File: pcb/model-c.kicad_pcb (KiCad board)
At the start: 2 copper layers, 82 x 144.9 mm, 157 parts, among them IC1 HTK16K33, IC2 HTK16K33, J1 Batt, J2 Conn_01x02_Socket, J3 Conn_01x02_Socket, SW1 SW_SPST, SW10 SW_SPST, SW11 SW_SPST, SW12 SW_SPST, SW13 SW_SPST, SW14 SW_SPST, SW15 SW_SPST, SW16 SW_SPST, SW17 SW_SPST, SW18 SW_SPST, SW19 SW_SPST, SW2 SW_SPST, SW21 SW_SPDT, SW3 SW_SPST, SW4 SW_SPST, SW5 SW_SPST, SW6 SW_SPST, SW7 SW_SPST, SW8 SW_SPST, SW9 SW_SPST, U1 W25Q16JVUXIQ, U11 TPS63070RNMR, U2 14seg, U3 RP2040, U4 MCP73831-2-OT, U5 TPS61090, U6 14seg, U7 TLV75533PDBVR, U8 TPS2115APW, U9 TPS2115APW, Y1 12MHz

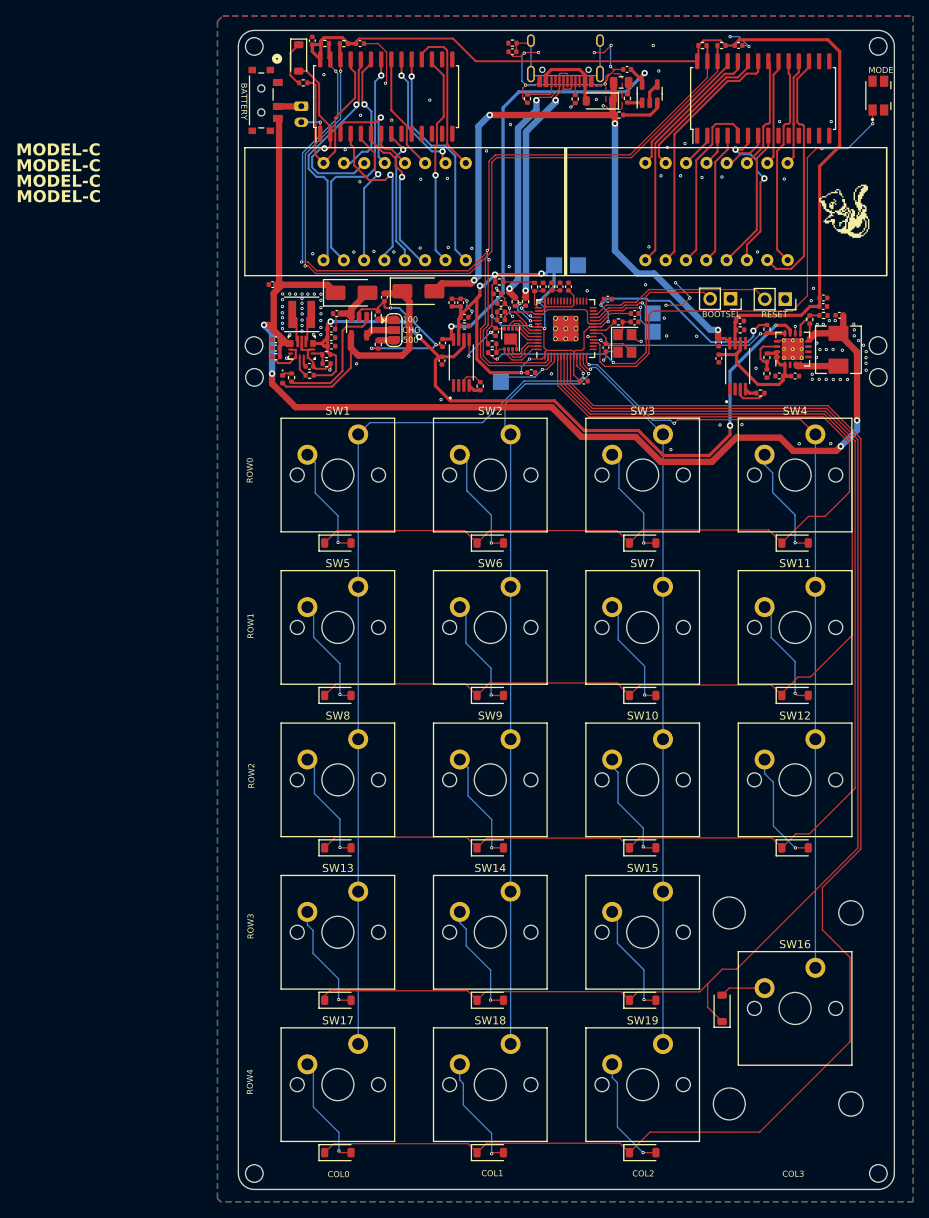
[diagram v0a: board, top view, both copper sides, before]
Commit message: housing complete and PCB validated. need further validation and revisions of housing, as well as BOM to continue. updated PCB to rev. 2.1
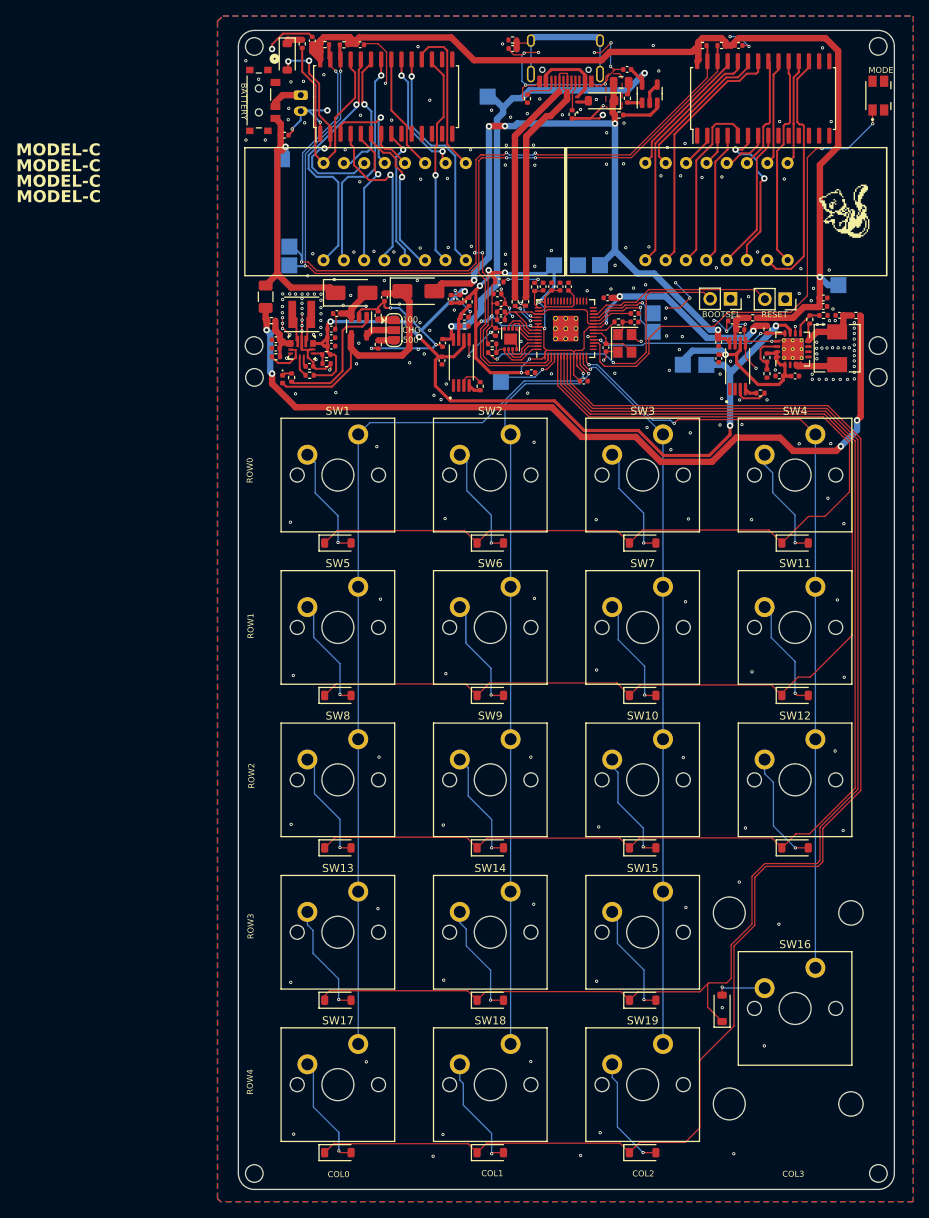
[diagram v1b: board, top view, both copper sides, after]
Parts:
- added D25: TPD1E05U06, footprints:RTVS_DFN1006-2_SOD882_NEX, F.Cu at (88.2, 33.3)
- added F2: Polyfuse_Small, Fuse:Fuse_1206_3216Metric, F.Cu at (49.2, 57.9)
- added FB2: FB, Resistor_SMD:R_0402_1005Metric, F.Cu at (110.1, 60.6)
- added FB3: FB, Resistor_SMD:R_0402_1005Metric, F.Cu at (74.7, 58.6)
- added FB4: FB, Resistor_SMD:R_0402_1005Metric, F.Cu at (123.0, 60.3)
- added FB5: FB, Resistor_SMD:R_0402_1005Metric, F.Cu at (50.0, 60.9)
- added TP10: TestPoint, libraries:CustomTestPoint, B.Cu at (104.3, 66.5)
- added TP11: TestPoint, libraries:CustomTestPoint, B.Cu at (120.8, 56.5)
- added TP12: TestPoint, libraries:CustomTestPoint, B.Cu at (52.2, 54.0)
- added TP13: TestPoint, libraries:CustomTestPoint, B.Cu at (52.2, 51.7)
- added TP5: TestPoint, libraries:CustomTestPoint, B.Cu at (51.3, 40.8)
- added TP6: TestPoint, libraries:CustomTestPoint, B.Cu at (91.0, 54.0)
- added TP7: TestPoint, libraries:CustomTestPoint, B.Cu at (77.0, 32.9)
- added TP8: TestPoint, libraries:CustomTestPoint, B.Cu at (101.4, 66.4)
- moved C20 18.7 mm to (51.6, 37.7), turned to 0 degrees
- moved R4 4.88 mm to (53.8, 26.3), turned to 90 degrees
- moved R6 1.96 mm to (87.6, 35.1)
- moved D20 1.44 mm to (51.9, 28.0)
- moved J1 1.38 mm to (53.6, 32.7)
- moved C36 0.99 mm to (107.5, 61.0), turned to 180 degrees
- moved C2 0.46 mm to (73.5, 58.2)
- moved C22 0.46 mm to (72.4, 58.2)
- moved C6 0.40 mm to (80.1, 26.9)
- moved R8 0.40 mm to (80.1, 25.8)
- moved SW21 0.30 mm to (48.4, 33.4)
- moved D21 0.26 mm to (91.2, 33.4)
- moved L1 0.25 mm to (120.7, 64.4)
- moved C12 0.16 mm to (92.0, 58.1), turned to 180 degrees
- moved R18 0.14 mm to (59.0, 26.4)
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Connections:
- C20 pad 1: /B+ -> Net-(D24-K)
- C26 pad 1: /B+ -> Net-(U5-VBAT)
- C34 pad 1: /B+ -> Net-(C34-Pad1)
- C35 pad 1: +3V3 -> Net-(U8-OUT)
- C36 pad 1: +5V -> Net-(U9-OUT)
- C37 pad 2: /B+ -> Net-(C34-Pad1)
- D21 pad 2: VBUS -> Net-(D21-A)
- D24 pad 1: /B+ -> Net-(D24-K)
- L1 pad 1: /B+ -> Net-(U5-VBAT)
- R23 pad 1: /B+ -> Net-(C34-Pad1)
- R26 pad 1: +3V3 -> Net-(U8-OUT)
- R27 pad 1: +5V -> Net-(U9-OUT)
- R5 pad 1: /B+ -> Net-(U5-VBAT)
- SW21 pad 3: /B+ -> Net-(D24-K)
- U11 pad 12: /B+ -> Net-(C34-Pad1)
- U11 pad 13: /B+ -> Net-(C34-Pad1)
- U5 pad 8: /B+ -> Net-(U5-VBAT)
- U8 pad 7: +3V3 -> Net-(U8-OUT)
- U9 pad 7: +5V -> Net-(U9-OUT)
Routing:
- net GND: track 129.1 -> 183.7 mm, vias 134 -> 264
- net /B+: track 153.4 -> 104.6 mm
- net Net-(D24-K): track 0.00 -> 33.2 mm, vias 0 -> 1
- net Net-(U5-VBAT): track 0.00 -> 10.0 mm
- net Net-(C34-Pad1): track 0.00 -> 8.63 mm
- net /5V_BATT: track 20.1 -> 26.6 mm, vias 0 -> 1
- net Net-(U8-OUT): track 0.00 -> 5.15 mm
- net /SDA: track 124.1 -> 129.2 mm, vias 4 -> 6
- net Net-(U9-OUT): track 0.00 -> 4.60 mm
- net +5V: track 123.5 -> 128.0 mm, vias 0 -> 1
- net Net-(IC2-ROW0/A2): track 26.1 -> 30.3 mm
- net /row3: track 175.9 -> 180.0 mm
- net Net-(D20-A): track 23.1 -> 27.0 mm, vias 1 -> 3
- net /row4: track 194.6 -> 190.9 mm
- net Net-(D20-K): track 5.76 -> 2.32 mm
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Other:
- board text added: "3.3V"
- board text added: "3.3V USB"
- board text added: "5V"
- board text added: "B+"
- board text added: "Model-C - V2.1 Brian Hill 2025 github.com/TrojanPinata/Model-C"
- board text added: "SCL"
- board text added: "SDA"
- board text added: "VSYS"
- board text removed: "Model-C - V2.0 Brian Hill 2025 github.com/TrojanPinata/Model-C"

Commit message: updates to pcb and addition of display code. I may rewrite the calculator code
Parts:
- removed D20: 1N4148, Diode_SMD:D_SOD-123
- removed R17, R18: 10k, Resistor_SMD:R_0402_1005Metric
- removed R19, R20: 4.7k, Resistor_SMD:R_0402_1005Metric
- removed U2, U6: 14seg, hk:14 seg
- added DS1: TDCG1060M, libraries2:DISPLAY_TDCG1060M, F.Cu at (66.4, 47.6)
- added DS2: TDCG1060M, libraries2:DISPLAY_TDCG1060M, F.Cu at (107.2, 47.6)
- added R33: 4.7k, Resistor_SMD:R_0402_1005Metric, F.Cu at (106.3, 26.6)
- added R34: 4.7k, Resistor_SMD:R_0402_1005Metric, F.Cu at (103.9, 26.7)
- added TP14: TestPoint, libraries:CustomTestPoint, B.Cu at (84.7, 44.7)
- added TP15: TestPoint, libraries:CustomTestPoint, B.Cu at (84.7, 42.2)
- added U10: TXS0102DCU, Package_SO:VSSOP-8_2.3x2mm_P0.5mm, F.Cu at (88.6, 37.8)
- F2: value Polyfuse_Small -> MF-NSMF075-2
- G***: moved to B.Cu
- moved TP12 30.1 mm to (75.2, 34.6)
- moved TP13 27.2 mm to (75.1, 37.0)
- moved C25 15.2 mm to (76.2, 27.8), turned to 90 degrees
- moved C24 8.19 mm to (100.3, 28.0), turned to -90 degrees
- moved TP7 1.59 mm to (78.3, 32.1)
- moved R4 1.31 mm to (54.1, 27.6), turned to 0 degrees
- moved C5 1.22 mm to (54.0, 26.5), turned to 180 degrees
- moved R11 0.54 mm to (83.4, 56.7)
- moved C10 0.54 mm to (84.5, 56.7)
- moved C13 0.52 mm to (87.6, 56.7)
- moved C18 0.52 mm to (85.5, 56.7)
- moved C11 0.52 mm to (86.6, 56.7)
- moved TP2 0.24 mm to (97.6, 59.8)
- moved D23 0.21 mm to (51.3, 68.0)
- turned G*** to 180 degrees
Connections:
- IC1 pad 15: unconnected-(IC1-ROW10/K8-Pad15) -> Net-(IC1-ROW10/K8)
- IC1 pad 16: unconnected-(IC1-ROW9/K7-Pad16) -> Net-(IC1-ROW9/K7)
- IC1 pad 23: Net-(IC1-ROW2/A0) -> unconnected-(IC1-ROW2/A0-Pad23)
- IC1 pad 24: Net-(IC1-ROW1/A1) -> unconnected-(IC1-ROW1/A1-Pad24)
- IC1 pad 25: Net-(IC1-ROW0/A2) -> unconnected-(IC1-ROW0/A2-Pad25)
- IC1 pad 26: /SCL -> /SCL_5V
- IC1 pad 27: /SDA -> /SDA_5V
- IC1 pad 6: Net-(IC1-COM4) -> unconnected-(IC1-COM4-Pad6)
- IC1 pad 7: Net-(IC1-COM5) -> unconnected-(IC1-COM5-Pad7)
- IC1 pad 8: Net-(IC1-COM6) -> unconnected-(IC1-COM6-Pad8)
- IC2 pad 15: unconnected-(IC2-ROW10/K8-Pad15) -> Net-(IC2-ROW10/K8)
- IC2 pad 16: unconnected-(IC2-ROW9/K7-Pad16) -> Net-(IC2-ROW9/K7)
- IC2 pad 24: Net-(IC2-ROW1/A1) -> unconnected-(IC2-ROW1/A1-Pad24)
- IC2 pad 25: Net-(IC2-ROW0/A2) -> unconnected-(IC2-ROW0/A2-Pad25)
- IC2 pad 26: /SCL -> /SCL_5V
- IC2 pad 27: /SDA -> /SDA_5V
- IC2 pad 6: Net-(IC2-COM4) -> unconnected-(IC2-COM4-Pad6)
- IC2 pad 7: Net-(IC2-COM5) -> unconnected-(IC2-COM5-Pad7)
- IC2 pad 8: Net-(IC2-COM6) -> unconnected-(IC2-COM6-Pad8)
- R4 pad 1: Net-(IC2-ROW0/A2) -> Net-(IC2-ROW2/A0)
- R4 pad 2: Net-(D20-K) -> +5V
- TP12 pad 1: /SCL -> /SCL_5V
- TP13 pad 1: /SDA -> /SDA_5V
- U3 pad 2: /SDA -> /SDA_3.3V
- U3 pad 3: /SCL -> /SCL_3.3V
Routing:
- net /SDA: track 129.2 -> 0.00 mm, vias 6 -> 0
- net /SCL: track 127.1 -> 0.00 mm, vias 4 -> 0
- net /SDA_5V: track 0.00 -> 64.3 mm, vias 0 -> 5
- net /SCL_5V: track 0.00 -> 63.4 mm, vias 0 -> 3
- net /SCL_3.3V: track 0.00 -> 50.6 mm, vias 0 -> 2
- net /SDA_3.3V: track 0.00 -> 45.8 mm, vias 0 -> 2
- net GND: track 183.7 -> 221.7 mm, vias 264 -> 317
- net Net-(IC2-ROW1/A1): track 31.3 -> 0.00 mm, vias 1 -> 0
- net Net-(IC1-ROW10/K8): track 0.00 -> 30.6 mm
- net Net-(IC2-ROW0/A2): track 30.3 -> 0.00 mm
- net Net-(IC1-ROW1/A1): track 30.3 -> 0.00 mm
- net Net-(IC1-ROW9/K7): track 0.00 -> 29.6 mm, vias 0 -> 1
- net +3V3: track 124.4 -> 152.7 mm, vias 13 -> 14
- net Net-(IC2-ROW10/K8): track 0.00 -> 26.4 mm, vias 0 -> 1
- net +5V: track 128.0 -> 152.4 mm, vias 1 -> 3
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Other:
- board text added: "SCL_3.3V"
- board text added: "SCL_5V"
- board text added: "SDA_3.3V"
- board text added: "SDA_5V"
